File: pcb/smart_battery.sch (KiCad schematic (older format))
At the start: 10 parts, among them J1 feather long, J2 feather short

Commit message: Laying out the schematic
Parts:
- added R1, R2: R2k, symbol Device:R
- added RP1, RP2: MP930-0.02-1, Caddock-MP930-0-0-*, symbol mp930:MP930-0.075-1
- added U1Batt, U2Solar: LTC4151CS-2PBF, Linear_Technology-LTC4151CS-2PBF-*, symbol eec:LTC4151CS-2PBF
- added U?: LM317_3PinPackage, symbol Regulator_Linear:LM317_3PinPackage
- gave numbers to parts that had none: 8
- renumbered J1 to J5, J2 to J6
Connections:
- net labels added: +24V, +48V, +5V, 10, 11, 12, 13, 5, 6, 9, CS, HTEN, HTOUT, POUT, PSET, PUSET, SOUT, SSET, SUSET
- net labels removed: F0, F1, F2, F3, F4, F5, F6
- wire segments 150 -> 99
- no-connect marks 0 -> 96
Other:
- note added: "Ethernet"
- note added: "Latching Battery"
- note added: "Latching Solar"
- note added: "M0 Data Logger"
- note added: "Power Relay"

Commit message: Added thermistors and RTC.  Most feather pinouts done
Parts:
- added J11: Conn_01x05_RTC, symbol Connector_Generic:Conn_01x05
- added J12: Conn_HtrTh, symbol Connector:Conn_01x02_Male
- added J13: Conn_BattTh, symbol Connector:Conn_01x02_Male
- added R3, R4: R10k, symbol Device:R
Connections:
- net labels added: ENCS, THBAT, THHTR, VPIN, VSPO, VSSO
- net labels removed: 10, 11, 12, 13, 5, 6, 9, A0, A1, A2, A3
- wire segments 99 -> 118
- no-connect marks 96 -> 97
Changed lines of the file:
@@
 AREF
 Text Label 3800 1450 0    50   ~ 0
-A0
+THHTR
 Text Label 3800 1550 0    50   ~ 0
-A1
+THBAT
 Text Label 3800 1650 0    50   ~ 0
-A2
+VSSO
 Text Label 3800 1750 0    50   ~ 0
-A3
+VSPO
 Text Label 3800 1850 0    50   ~ 0
 A4
@@
 VUSB
 Text Label 5050 1750 2    50   ~ 0
-13
+VPIN
 Text Label 5050 1850 2    50   ~ 0
-12
+HTEN
 Text Label 5050 1950 2    50   ~ 0
-11
+SSET
 Text Label 5050 2050 2    50   ~ 0
-10
+ENCS
 Text Label 5050 2150 2    50   ~ 0
-9
+PUSET
 Text Label 5050 2250 2    50   ~ 0
-6
+PSET
 Text Label 5050 2350 2    50   ~ 0
-5
+SUSET
 Text Label 5050 2450 2    50   ~ 0
 SCL
@@
 Wire Wire Line
 	6350 4550 6550 4550
+$Comp
+L power:GND #PWR?
+U 1 1 6015681A
+P 1200 4150
+F 0 "#PWR?" H 1200 3900 50  0001 C CNN
+F 1 "GND" H 1205 3977 50  0000 C CNN
+F 2 "" H 1200 4150 50  0001 C CNN
+F 3 "" H 1200 4150 50  0001 C CNN
+	1    1200 4150
+	1    0    0    -1
+$EndComp
+Wire Wire Line
+	1400 4200 1350 4200
+Wire Wire Line
+	1350 4200 1350 4150
+Wire Wire Line
+	1350 4150 1200 4150
+$Comp
+L power:GND #PWR?
+U 1 1 6015AA91
+P 1400 5950
+F 0 "#PWR?" H 1400 5700 50  0001 C CNN
+F 1 "GND" H 1405 5777 50  0000 C CNN
+F 2 "" H 1400 5950 50  0001 C CNN
+F 3 "" H 1400 5950 50  0001 C CNN
+	1    1400 5950
+	1    0    0    -1
+$EndComp
+Wire Wire Line
+	1500 6250 1500 5950
+Wire Wire Line
+	1500 5950 1400 5950
+$Comp
+L Connector_Generic:Conn_01x05 J11
+U 1 1 60127D8D
+P 8100 5650
+F 0 "J11" H 8180 5692 50  0000 L CNN
+F 1 "Conn_01x05_RTC" H 8180 5601 50  0000 L CNN
+F 2 "" H 8100 5650 50  0001 C CNN
+F 3 "~" H 8100 5650 50  0001 C CNN
+	1    8100 5650
+	1    0    0    -1
+$EndComp
+Text Label 7750 5550 0    50   ~ 0
+VPIN
+Text Label 7750 5650 0    50   ~ 0
+SDA
+Text Label 7750 5750 0    50   ~ 0
+SCL
+NoConn ~ 7900 5850
+$Comp
+L power:GND #PWR?
+U 1 1 6012C796
+P 7600 5450
+F 0 "#PWR?" H 7600 5200 50  0001 C CNN
+F 1 "GND" H 7605 5277 50  0000 C CNN
+F 2 "" H 7600 5450 50  0001 C CNN
+F 3 "" H 7600 5450 50  0001 C CNN
+	1    7600 5450
+	1    0    0    -1
+$EndComp
+Wire Wire Line
+	7600 5450 7900 5450
+Wire Wire Line
+	7750 5550 7900 5550
+Wire Wire Line
+	7750 5650 7900 5650
+Wire Wire Line
+	7750 5750 7900 5750
+$Comp
+L Device:R R3
+U 1 1 6013ECC6
+P 1500 1850
+F 0 "R3" H 1570 1896 50  0000 L CNN
+F 1 "R10k" H 1570 1805 50  0000 L CNN
+F 2 "" V 1430 1850 50  0001 C CNN
+F 3 "~" H 1500 1850 50  0001 C CNN
+	1    1500 1850
+	1    0    0    -1
+$EndComp
+$Comp
+L Device:R R4
+U 1 1 6013ED4E
+P 1800 1850
+F 0 "R4" H 1870 1896 50  0000 L CNN
+F 1 "R10k" H 1870 1805 50  0000 L CNN
+F 2 "" V 1730 1850 50  0001 C CNN
+F 3 "~" H 1800 1850 50  0001 C CNN
+	1    1800 1850
+	1    0    0    -1
+$EndComp
+Text Label 1500 1500 0    50   ~ 0
+VPIN
+Wire Wire Line
+	1500 1500 1500 1550
+Wire Wire Line
+	1500 1550 1800 1550
+Wire Wire Line
+	1800 1550 1800 1700
+Connection ~ 1500 1550
+Wire Wire Line
+	1500 1550 1500 1700
+$Comp
+L Connector:Conn_01x02_Male J12
+U 1 1 60148FF6
+P 1300 2250
+F 0 "J12" H 1406 2428 50  0000 C CNN
+F 1 "Conn_HtrTh" H 1406 2337 50  0000 C CNN
+F 2 "" H 1300 2250 50  0001 C CNN
+F 3 "~" H 1300 2250 50  0001 C CNN
+	1    1300 2250
+	1    0    0    -1
+$EndComp
+$Comp
+L Connector:Conn_01x02_Male J13
+U 1 1 60149078
+P 2000 2350
+F 0 "J13" H 1973 2230 50  0000 R CNN
+F 1 "Conn_BattTh" H 1973 2321 50  0000 R CNN
+F 2 "" H 2000 2350 50  0001 C CNN
+F 3 "~" H 2000 2350 50  0001 C CNN
+	1    2000 2350
+	-1   0    0    1
+$EndComp
+$Comp
+L power:GND #PWR?
+U 1 1 60149136
+P 1650 2500
+F 0 "#PWR?" H 1650 2250 50  0001 C CNN
+F 1 "GND" H 1655 2327 50  0000 C CNN
+F 2 "" H 1650 2500 50  0001 C CNN
+F 3 "" H 1650 2500 50  0001 C CNN
+	1    1650 2500
+	1    0    0    -1
+$EndComp
+Wire Wire Line
+	1500 2350 1500 2500
+Wire Wire Line
+	1500 2500 1650 2500
+Wire Wire Line
+	1800 2350 1800 2500
+Wire Wire Line
+	1800 2500 1650 2500
+Connection ~ 1650 2500
+Text Label 1800 2100 0    50   ~ 0
+THBAT
+Text Label 1500 2100 0    50   ~ 0
+THHTR
+Wire Wire Line
+	1500 2000 1500 2250
+Wire Wire Line
+	1800 2000 1800 2250
 $EndSCHEMATC

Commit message: Added 3.3 volt ethernet circuit
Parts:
- removed U?: LM317_3PinPackage, symbol Regulator_Linear:LM317_3PinPackage
- added C? (x2): C10uF, symbol Device:C
- added C?: C1uF, symbol Device:C
- added J14: PowerRelay, symbol Connector:Conn_01x02_Male
- added J15: SolarRelay, symbol Connector:Conn_01x02_Male
- added R?: 100K, symbol Device:R_Small
- added U?: SPX3819M5-L-3-3, Package_TO_SOT_SMD:SOT-23-5, symbol Regulator_Linear:SPX3819M5-L-3-3
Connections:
- net labels added: Eth3.3
- net labels removed: HTOUT
- wire segments 118 -> 122
- no-connect marks 97 -> 105
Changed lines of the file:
@@
 	9650 1950 9900 1950
-$Comp
-L power:+3.3V #PWR01
-U 1 1 5D37877D
-P 8500 950
-F 0 "#PWR01" H 8500 800 50  0001 C CNN
-F 1 "+3.3V" H 8515 1123 50  0000 C CNN
-F 2 "" H 8500 950 50  0001 C CNN
-F 3 "" H 8500 950 50  0001 C CNN
-	1    8500 950
-	1    0    0    -1
-$EndComp
 $Comp
 L power:GND #PWR02
@@
 	1    0    0    -1
 $EndComp
-Wire Wire Line
-	8500 950  8500 1050
 Wire Wire Line
 	8500 1050 8850 1050
@@
 	3800 3600 4000 3600
 $Comp
-L power:+3.3V #PWR?
-U 1 1 600BEE44
-P 3650 3600
-F 0 "#PWR?" H 3650 3450 50  0001 C CNN
-F 1 "+3.3V" H 3665 3773 50  0000 C CNN
-F 2 "" H 3650 3600 50  0001 C CNN
-F 3 "" H 3650 3600 50  0001 C CNN
-	1    3650 3600
-	1    0    0    -1
-$EndComp
-$Comp
-L power:GND #PWR?
-U 1 1 600BEE4A
-P 3650 4000
-F 0 "#PWR?" H 3650 3750 50  0001 C CNN
-F 1 "GND" H 3655 3827 50  0000 C CNN
-F 2 "" H 3650 4000 50  0001 C CNN
-F 3 "" H 3650 4000 50  0001 C CNN
-	1    3650 4000
-	1    0    0    -1
-$EndComp
-Wire Wire Line
-	3650 3600 3650 3700
-Wire Wire Line
-	3650 3700 4000 3700
-Wire Wire Line
-	3650 4000 3650 3900
-Wire Wire Line
-	3650 3900 4000 3900
-$Comp
 L Connector_Generic:Conn_01x16 J9
 U 1 1 600C6BA0
@@
 Wire Wire Line
 	6350 3550 6550 3550
-$Comp
-L power:+3.3V #PWR?
-U 1 1 600C6BE2
-P 6200 3550
-F 0 "#PWR?" H 6200 3400 50  0001 C CNN
-F 1 "+3.3V" H 6215 3723 50  0000 C CNN
-F 2 "" H 6200 3550 50  0001 C CNN
-F 3 "" H 6200 3550 50  0001 C CNN
-	1    6200 3550
-	1    0    0    -1
-$EndComp
-$Comp
-L power:GND #PWR?
-U 1 1 600C6BE8
-P 6200 3950
-F 0 "#PWR?" H 6200 3700 50  0001 C CNN
-F 1 "GND" H 6205 3777 50  0000 C CNN
-F 2 "" H 6200 3950 50  0001 C CNN
-F 3 "" H 6200 3950 50  0001 C CNN
-	1    6200 3950
-	1    0    0    -1
-$EndComp
-Wire Wire Line
-	6200 3550 6200 3650
-Wire Wire Line
-	6200 3650 6550 3650
-Wire Wire Line
-	6200 3950 6200 3850
-Wire Wire Line
-	6200 3850 6550 3850
 $Comp
 L power:+5V #PWR?
@@
 NoConn ~ 7250 1800
 NoConn ~ 7250 1700
-NoConn ~ 7250 1600
 NoConn ~ 7250 1500
 NoConn ~ 7250 1400
 NoConn ~ 8850 1350
-Text Label 6300 1400 0    50   ~ 0
-HTEN
-Wire Wire Line
-	6300 1400 6450 1400
-Text Label 3750 4400 0    50   ~ 0
-SUSET
 NoConn ~ 4000 4700
 NoConn ~ 4000 4800
@@
 NoConn ~ 4800 4600
 NoConn ~ 4800 4700
-NoConn ~ 4800 4800
-NoConn ~ 4800 4900
 NoConn ~ 4800 5000
 NoConn ~ 4800 5100
@@
 NoConn ~ 7350 4050
 NoConn ~ 7350 3950
-$Comp
-L Regulator_Linear:LM317_3PinPackage U?
-U 1 1 6025DD67
-P 9150 4500
-F 0 "U?" H 9150 4742 50  0000 C CNN
-F 1 "LM317_3PinPackage" H 9150 4651 50  0000 C CNN
-F 2 "" H 9150 4750 50  0001 C CIN
-F 3 "http://www.ti.com/lit/ds/symlink/lm317.pdf" H 9150 4500 50  0001 C CNN
-	1    9150 4500
-	1    0    0    -1
-$EndComp
 $Comp
 L eec:LTC4151CS-2PBF U1Batt
@@
 	4800 2550 5600 2550
 $Comp
-L power:+24V #PWR?
-U 1 1 6012D930
-P 6250 1700
-F 0 "#PWR?" H 6250 1550 50  0001 C CNN
-F 1 "+24V" H 6265 1873 50  0000 C CNN
-F 2 "" H 6250 1700 50  0001 C CNN
-F 3 "" H 6250 1700 50  0001 C CNN
-	1    6250 1700
-	1    0    0    -1
-$EndComp
-Wire Wire Line
-	6250 1700 6450 1700
-Text Label 6250 1800 0    50   ~ 0
-HTOUT
-Wire Wire Line
-	6250 1800 6450 1800
-Wire Wire Line
-	3750 4400 4000 4400
-Text Label 3750 4300 0    50   ~ 0
-SSET
-Wire Wire Line
-	4000 4300 3750 4300
-$Comp
 L power:+5V #PWR?
 U 1 1 60141A92
@@
 Wire Wire Line
 	1800 2000 1800 2250
+Text Label 7400 1600 0    50   ~ 0
+HTEN
+Wire Wire Line
+	7400 1600 7250 1600
+NoConn ~ 6450 1400
+NoConn ~ 6450 1700
+NoConn ~ 6450 1800
+Wire Wire Line
+	3750 4400 4000 4400
+Text Label 3750 4400 0    50   ~ 0
+SUSET
+Wire Wire Line
+	4000 4300 3750 4300
+Text Label 3750 4300 0    50   ~ 0
+SSET
+NoConn ~ 4800 4800
+NoConn ~ 4800 4900
+$Comp
+L Connector:Conn_01x02_Male J15
+U 1 1 60168A13
+P 4950 5450
+F 0 "J15" H 4923 5330 50  0000 R CNN
+F 1 "SolarRelay" H 4923 5421 50  0000 R CNN
+F 2 "" H 4950 5450 50  0001 C CNN
+F 3 "~" H 4950 5450 50  0001 C CNN
+	1    4950 5450
+	-1   0    0    1
+$EndComp
+$Comp
+L power:GND #PWR?
+U 1 1 60168CFD
+P 4750 5450
+F 0 "#PWR?" H 4750 5200 50  0001 C CNN
+F 1 "GND" H 4755 5277 50  0000 C CNN
+F 2 "" H 4750 5450 50  0001 C CNN
+F 3 "" H 4750 5450 50  0001 C CNN
+	1    4750 5450
+	1    0    0    -1
+$EndComp
+Text Label 4550 5350 0    50   ~ 0
+SOUT
+Wire Wire Line
+	4550 5350 4750 5350
+$Comp
+L Connector:Conn_01x02_Male J14
+U 1 1 6016DE35
+P 7000 5500
+F 0 "J14" H 6973 5380 50  0000 R CNN
+F 1 "PowerRelay" H 6973 5471 50  0000 R CNN
+F 2 "" H 7000 5500 50  0001 C CNN
+F 3 "~" H 7000 5500 50  0001 C CNN
+	1    7000 5500
+	-1   0    0    1
+$EndComp
+$Comp
+L power:GND #PWR?
+U 1 1 6016DE3C
+P 6800 5500
+F 0 "#PWR?" H 6800 5250 50  0001 C CNN
+F 1 "GND" H 6805 5327 50  0000 C CNN
+F 2 "" H 6800 5500 50  0001 C CNN
+F 3 "" H 6800 5500 50  0001 C CNN
+	1    6800 5500
+	1    0    0    -1
+$EndComp
+Text Label 6600 5400 0    50   ~ 0
+POUT
+Wire Wire Line
+	6600 5400 6800 5400
+NoConn ~ 4000 3900
+NoConn ~ 4000 3700
+NoConn ~ 6550 3850
+NoConn ~ 6550 3750
+NoConn ~ 6550 3650
+$Comp
+L Regulator_Linear:SPX3819M5-L-3-3 U?
+U 1 1 60178915
+P 9100 3450
+F 0 "U?" H 9100 3792 50  0000 C CNN
+F 1 "SPX3819M5-L-3-3" H 9100 3701 50  0000 C CNN
+F 2 "Package_TO_SOT_SMD:SOT-23-5" H 9100 3775 50  0001 C CNN
+F 3 "https://www.exar.com/content/document.ashx?id=22106&languageid=1033&type=Datasheet&partnumber=SPX3819&filename=SPX3819.pdf&part=SPX3819" H 9100 3450 50  0001 C CNN
+	1    9100 3450
+	1    0    0    -1
+$EndComp
+$Comp
+L power:GND #PWR?
+U 1 1 60178A97
+P 9100 3750
+F 0 "#PWR?" H 9100 3500 50  0001 C CNN
+F 1 "GND" H 9105 3577 50  0000 C CNN
+F 2 "" H 9100 3750 50  0001 C CNN
+F 3 "" H 9100 3750 50  0001 C CNN
+	1    9100 3750
+	1    0    0    -1
+$EndComp
+$Comp
+L Device:C C?
+U 1 1 60178C04
+P 9550 3600
+F 0 "C?" H 9665 3646 50  0000 L CNN
+F 1 "C10uF" H 9665 3555 50  0000 L CNN
+F 2 "" H 9588 3450 50  0001 C CNN
+F 3 "~" H 9550 3600 50  0001 C CNN
+	1    9550 3600
+	1    0    0    -1
+$EndComp
+$Comp
+L Device:C C?
+U 1 1 60178CA6
+P 9900 3600
+F 0 "C?" H 10015 3646 50  0000 L CNN
+F 1 "C1uF" H 10015 3555 50  0000 L CNN
+F 2 "" H 9938 3450 50  0001 C CNN
+F 3 "~" H 9900 3600 50  0001 C CNN
+	1    9900 3600
+	1    0    0    -1
+$EndComp
+$Comp
+L power:GND #PWR?
+U 1 1 60178D25
+P 9550 3850
+F 0 "#PWR?" H 9550 3600 50  0001 C CNN
+F 1 "GND" H 9555 3677 50  0000 C CNN
+F 2 "" H 9550 3850 50  0001 C CNN
+F 3 "" H 9550 3850 50  0001 C CNN
+	1    9550 3850
+	1    0    0    -1
+$EndComp
+Wire Wire Line
+	9550 3850 9550 3750
+Wire Wire Line
+	9550 3750 9900 3750
+Connection ~ 9550 3750
+Wire Wire Line
+	9400 3350 9550 3350
+Wire Wire Line
+	9550 3350 9550 3450
+Wire Wire Line
+	9550 3350 9900 3350
+Wire Wire Line
+	9900 3350 9900 3450
+Connection ~ 9550 3350
+Text Label 10000 3350 0    50   ~ 0
+Eth3.3
+Wire Wire Line
+	10000 3350 9900 3350
+Connection ~ 9900 3350
+Text Label 8500 1050 0    50   ~ 0
+Eth3.3
+NoConn ~ 9400 3450
+$Comp
+L Device:R_Small R?
+U 1 1 601A923F
+P 8600 3550
+F 0 "R?" V 8404 3550 50  0000 C CNN
+F 1 "100K" V 8495 3550 50  0000 C CNN
+F 2 "" H 8600 3550 50  0001 C CNN
+F 3 "~" H 8600 3550 50  0001 C CNN
+	1    8600 3550
+	0    1    1    0
+$EndComp
+Wire Wire Line
+	8500 3200 8500 3350
+Wire Wire Line
+	8500 3350 8800 3350
+Wire Wire Line
+	8500 3350 8500 3550
+Connection ~ 8500 3350
+Wire Wire Line
+	8700 3550 8700 3450
+Wire Wire Line
+	8700 3450 8800 3450
+$Comp
+L Device:C C?
+U 1 1 601B844F
+P 8500 3700
+F 0 "C?" H 8615 3746 50  0000 L CNN
+F 1 "C10uF" H 8615 3655 50  0000 L CNN
+F 2 "" H 8538 3550 50  0001 C CNN
+F 3 "~" H 8500 3700 50  0001 C CNN
+	1    8500 3700
+	1    0    0    -1
+$EndComp
+Connection ~ 8500 3550
+$Comp
+L power:GND #PWR?
+U 1 1 601B8538
+P 8500 3850
+F 0 "#PWR?" H 8500 3600 50  0001 C CNN
+F 1 "GND" H 8505 3677 50  0000 C CNN
+F 2 "" H 8500 3850 50  0001 C CNN
+F 3 "" H 8500 3850 50  0001 C CNN
+	1    8500 3850
+	1    0    0    -1
+$EndComp
+Text Label 8300 3200 0    50   ~ 0
+POUT
+Wire Wire Line
+	8300 3200 8500 3200
 $EndSCHEMATC

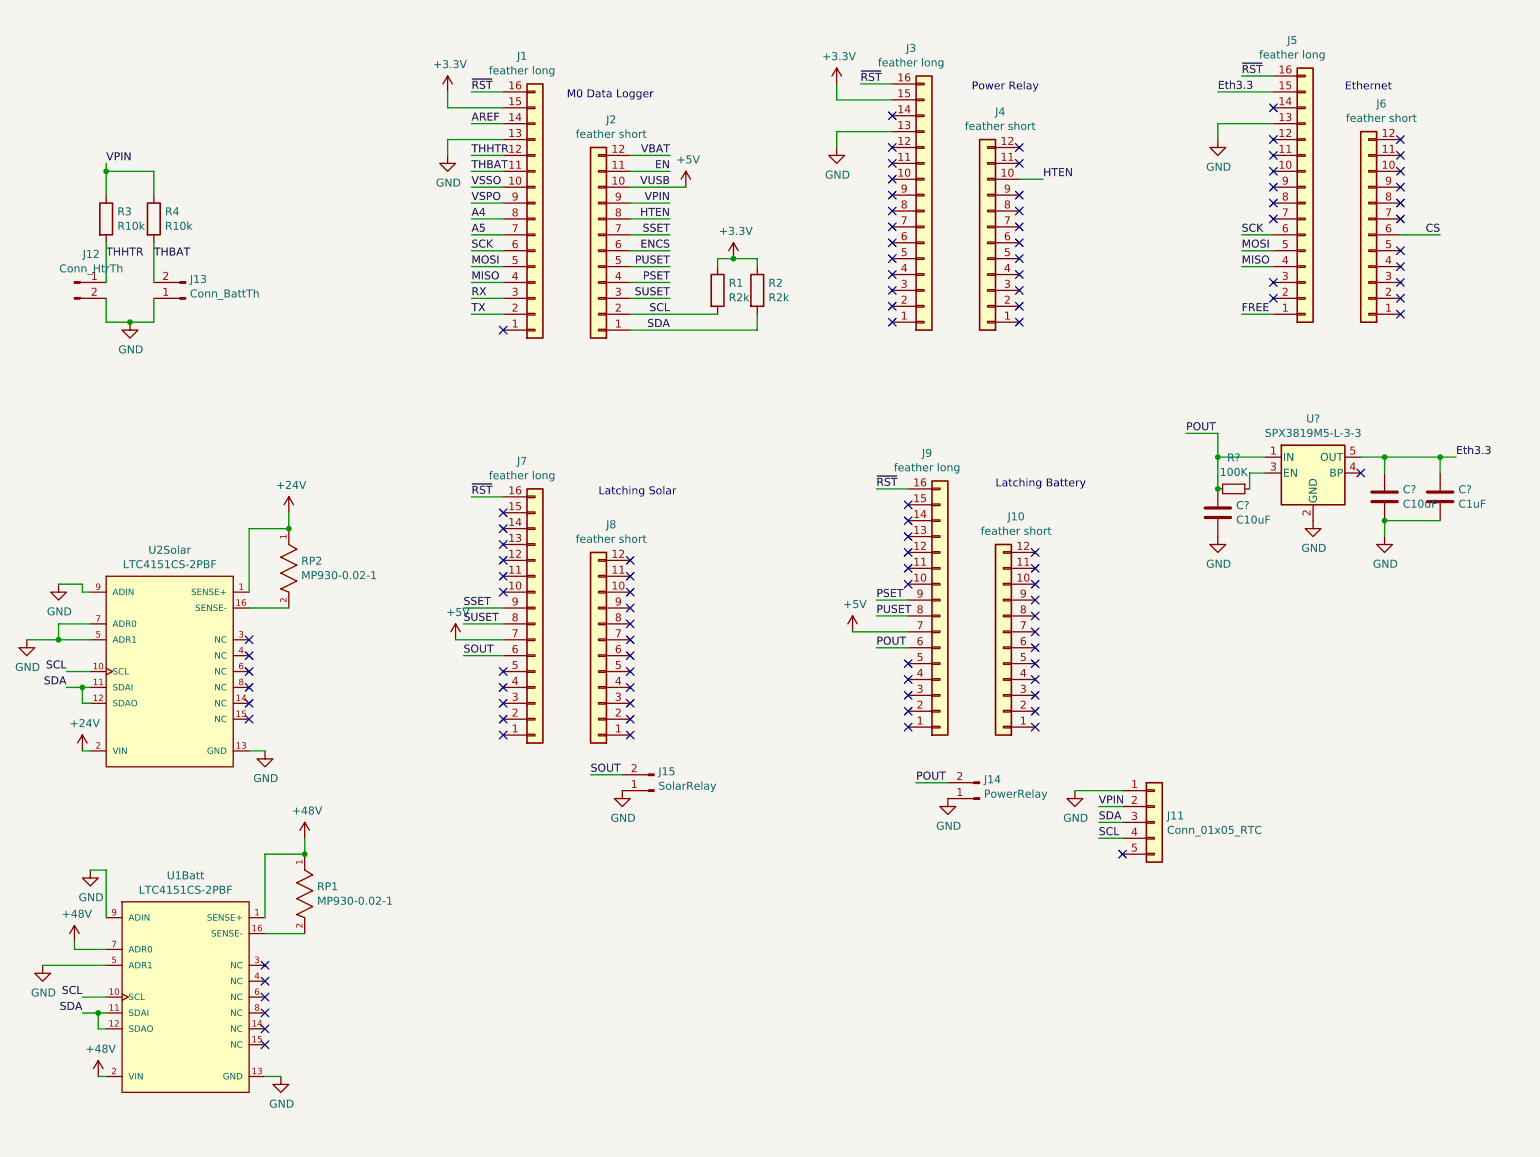
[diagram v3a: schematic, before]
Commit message: Added connectors and start the PCB
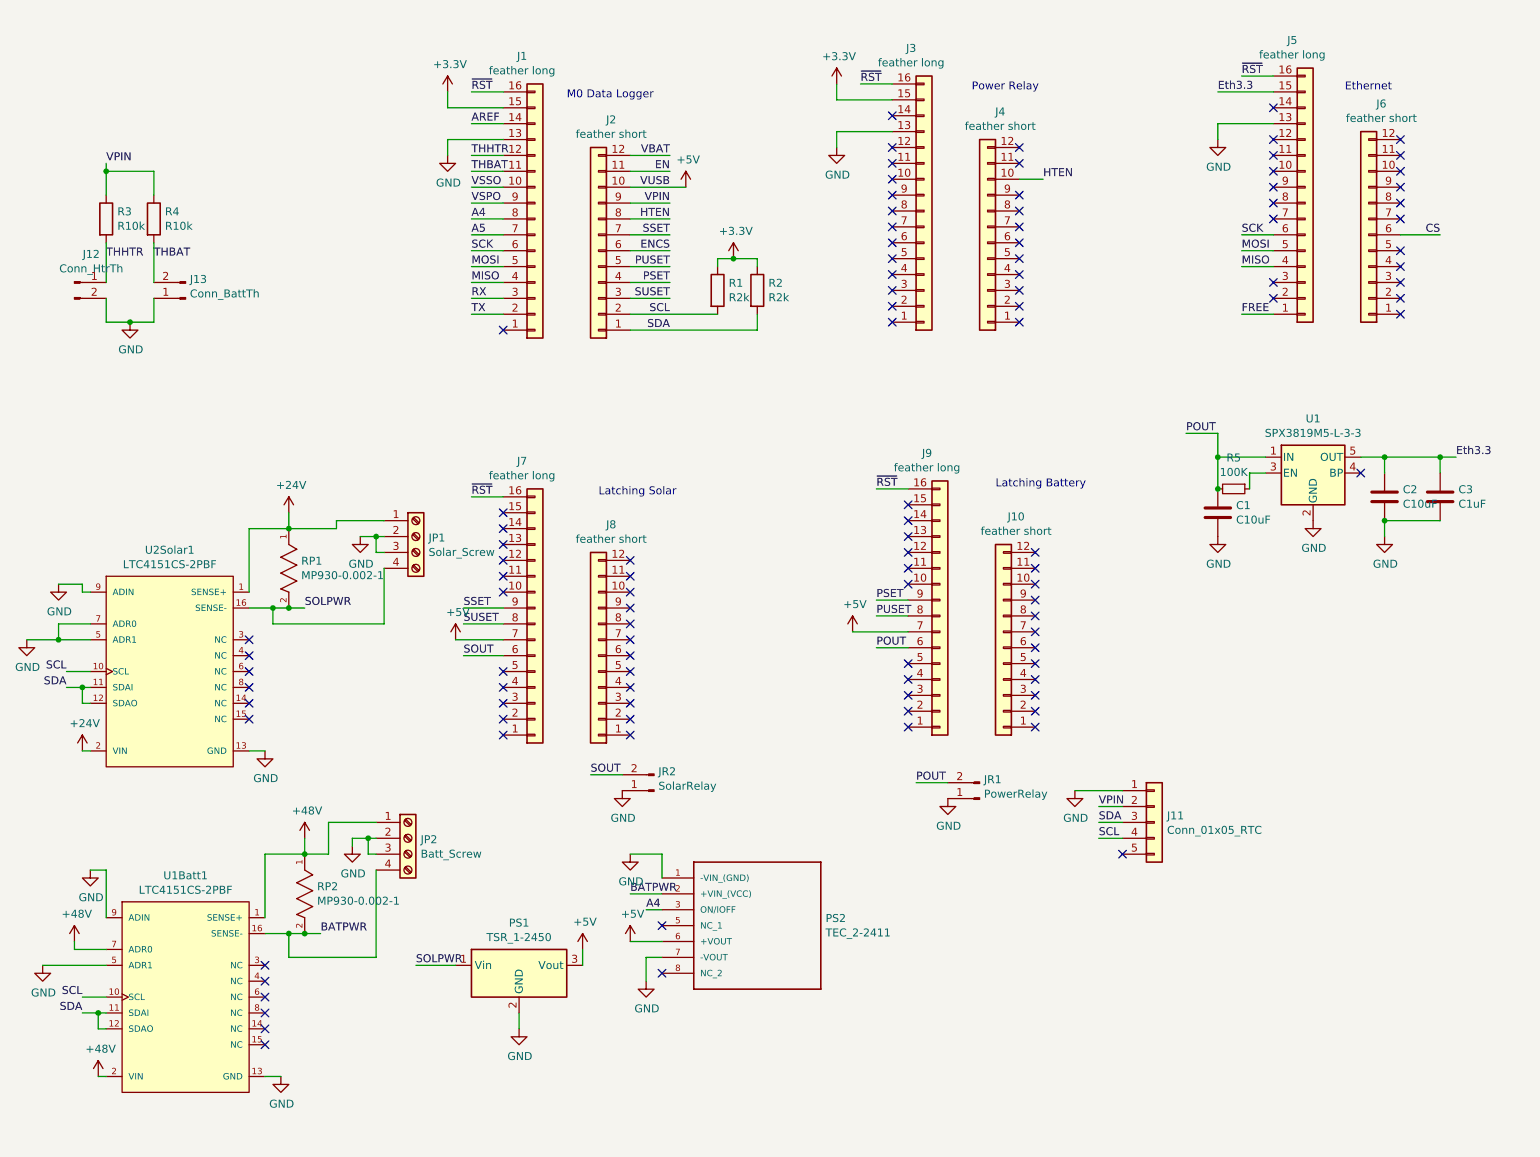
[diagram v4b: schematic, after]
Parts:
- removed RP1, RP2: MP930-0.02-1, Caddock-MP930-0-0-*, symbol mp930:MP930-0.075-1
- added JP1: Solar_Screw, symbol Connector:Screw_Terminal_01x04
- added JP2: Batt_Screw, symbol Connector:Screw_Terminal_01x04
- added PS1: TSR_1-2450, Converter_DCDC:Converter_DCDC_TRACO_TSR-1_THT, symbol Regulator_Switching:TSR_1-2450
- added PS2: TEC_2-2411, TEC_2:TEC24811, symbol TEC_2-2411:TEC_2-2411
- added RP1, RP2: MP930-0.002-1, mp930:Caddock-MP930-0-0-Recommended_Land_Pattern_, symbol mp930:MP930-0.002-1
- J11: footprint (none) -> Connector_PinHeader_2.54mm:PinHeader_1x05_P2.54mm_Vertical
- U1Batt1: renamed from U1Batt; footprint Linear_Technology-LTC4151CS-2PBF-* -> eec:Linear_Technology-LTC4151CS-2PBF-Level_B
- U2Solar1: renamed from U2Solar; footprint Linear_Technology-LTC4151CS-2PBF-* -> eec:Linear_Technology-LTC4151CS-2PBF-Level_B
- gave numbers to parts that had none: 5
- renumbered J14 to JR1, J15 to JR2
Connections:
- net +24V: now also JP1.1 (Pin_1), RP1.1
- net +48V: now also JP2.1 (Pin_1), RP2.1
- net +5V: now also PS1.3 (Vout), PS2.6 (+VOUT)
- net A4: now also PS2.3 (ON/IOFF)
- net GND: now also JP1.2 (Pin_2), JP1.3 (Pin_3), JP2.2 (Pin_2), JP2.3 (Pin_3), PS1.2 (GND), PS2.1 (-VIN_(GND)), PS2.7 (-VOUT)
- net BATPWR: now reaches U1Batt1.16 (SENSE-)
- net BATPWR: now also JP2.4 (Pin_4), PS2.2 (+VIN_(VCC)), RP2.2
- net SOLPWR: now reaches U2Solar1.16 (SENSE-)
- net SOLPWR: now also JP1.4 (Pin_4), PS1.1 (Vin), RP1.2
- no-connect marks 105 -> 107
